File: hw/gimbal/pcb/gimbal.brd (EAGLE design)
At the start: 60 x 42 mm, 79 parts, among them J1 JST-XH4SMT_RA, U1 STM32F4R_64PIN, U2 TPS62172PWSON8, U3 TPS55330PQFN16, U4 MC33926, U5 DRV8313, U6 DRV8313, U7 AS5048A

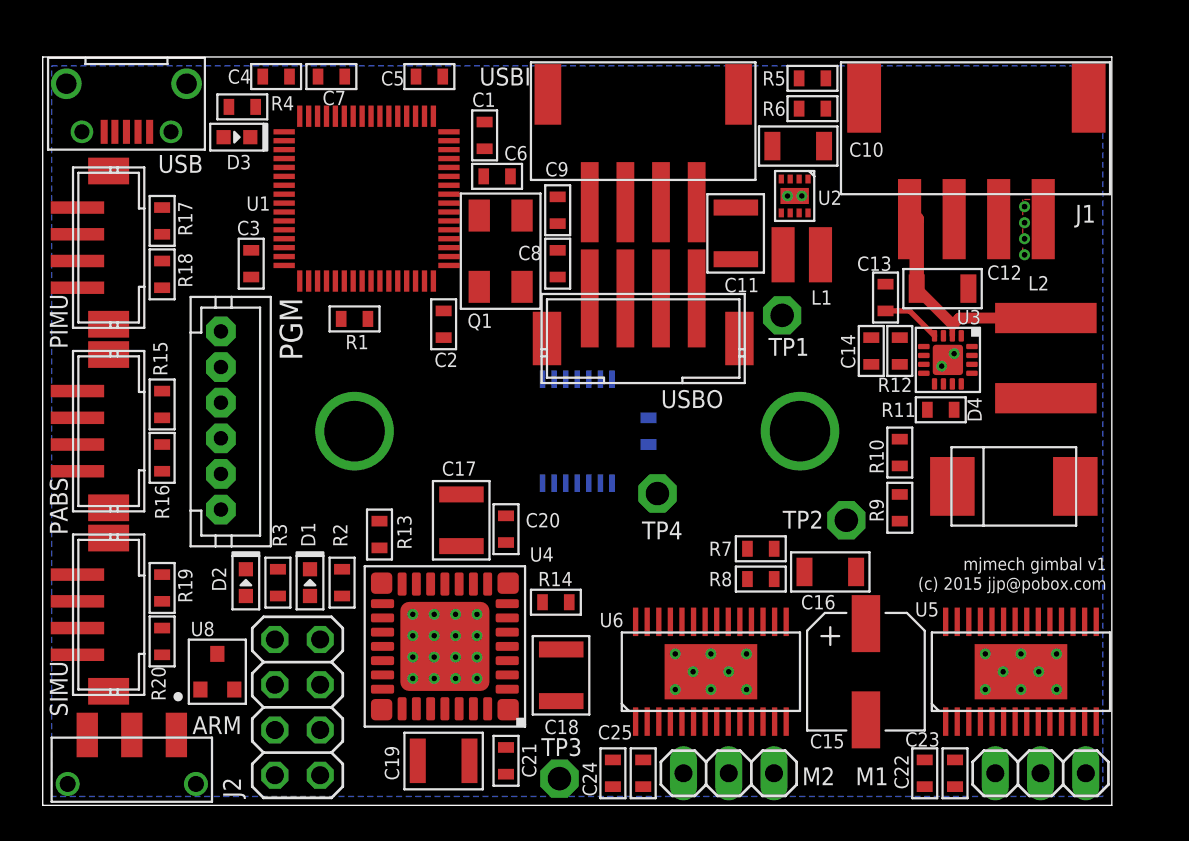
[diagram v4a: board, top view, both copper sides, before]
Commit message: gimbal board: Continued work on routing power.
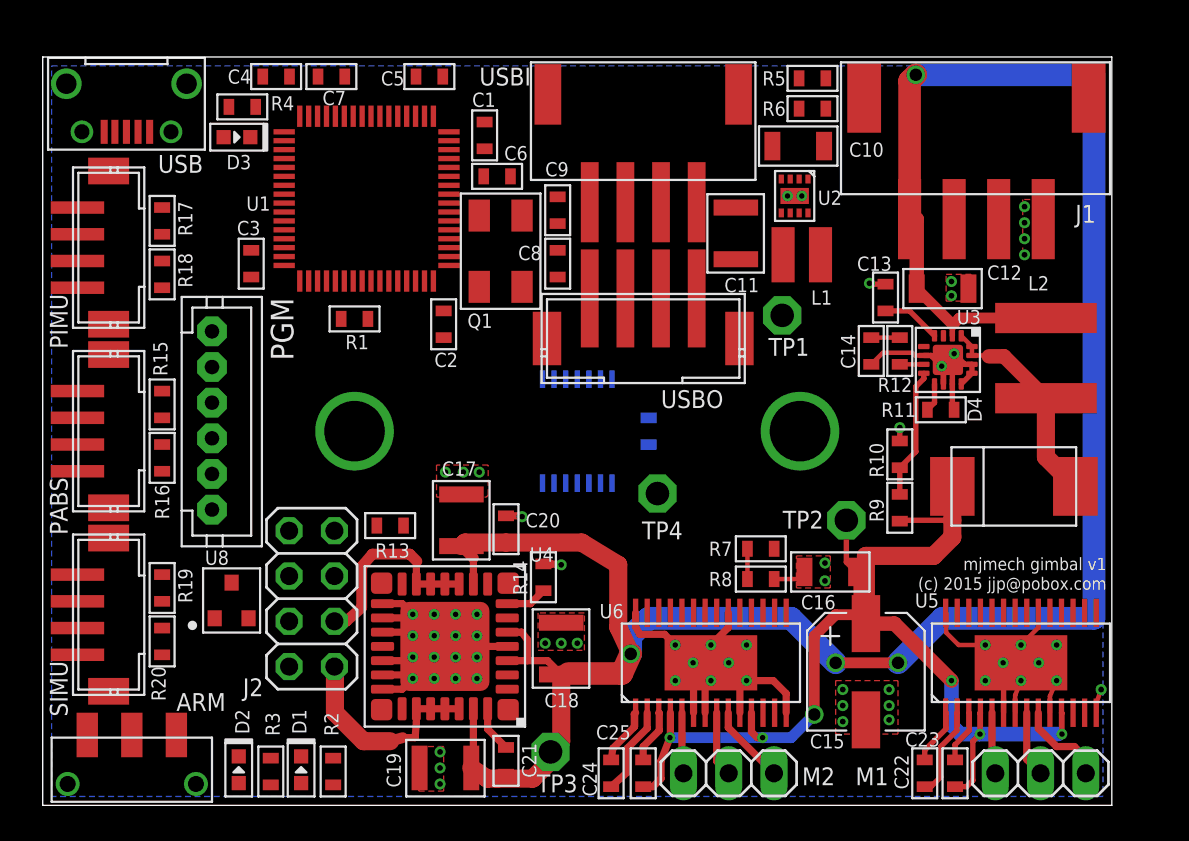
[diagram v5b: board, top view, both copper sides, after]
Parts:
- moved R2 10.6 mm to (16.3, 1.90)
- moved R3 10.6 mm to (12.8, 1.90)
- moved D1 10.5 mm to (14.5, 2.00)
- moved D2 10.5 mm to (11.0, 2.00)
- moved J2 6.15 mm to (15.1, 11.6)
- moved U8 4.08 mm to (10.6, 11.5)
- moved TP3 1.58 mm to (28.5, 3.00)
- moved R14 1.57 mm to (28.1, 12.8), turned to 270 degrees
- moved C18 1.50 mm to (29.1, 8.80)
- moved R13 0.78 mm to (19.5, 15.7), turned to 0 degrees
- moved PGM 0.50 mm to (9.50, 21.6)
- moved U5 0.50 mm to (54.9, 8.00)
- moved U6 0.50 mm to (37.5, 8.00)
- moved C19 0.41 mm to (22.6, 2.10)
- moved C25 0.10 mm to (31.9, 1.80)
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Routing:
- net +8V: track 13.2 -> 133.4 mm, vias 0 -> 4
- net +12V: track 0.00 -> 65.2 mm, vias 0 -> 6
- net GND: track 0.00 -> 61.6 mm, vias 4 -> 28
- net N$17: track 0.00 -> 12.1 mm
- net N$3: track 0.00 -> 11.8 mm
- net N$2: track 0.00 -> 11.4 mm
- net N$22: track 0.00 -> 7.36 mm
- net N$27: track 0.00 -> 5.11 mm
- net N$8: track 0.00 -> 5.09 mm
- net N$26: track 0.00 -> 5.02 mm
- net N$11: track 0.00 -> 4.46 mm
- net N$7: track 0.00 -> 3.72 mm
- net N$10: track 0.00 -> 3.68 mm
- net N$6: track 0.00 -> 3.48 mm
- net N$9: track 0.00 -> 3.44 mm
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
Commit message: gimbal board: More power routing.  Most ground pins have vias down to the ground plane now.
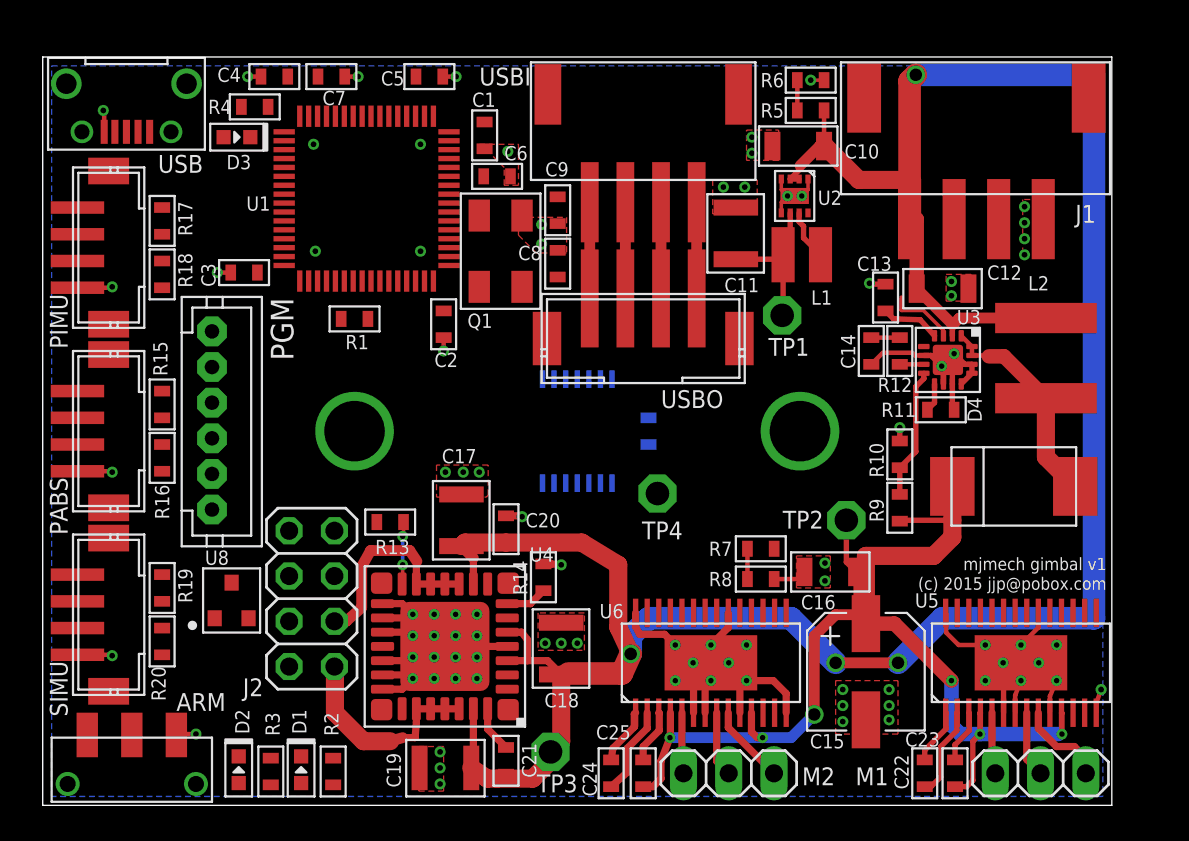
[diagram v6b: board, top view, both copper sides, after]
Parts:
- moved R5 1.80 mm to (43.1, 39.0)
- moved R6 1.60 mm to (43.1, 40.7)
- moved R4 0.70 mm to (11.9, 39.2)
- moved C3 0.64 mm to (11.3, 29.9), turned to 180 degrees
- moved R13 0.20 mm to (19.5, 15.9)
- moved C4 0.10 mm to (13.0, 40.9), turned to 180 degrees
- turned C10 to 180 degrees
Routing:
- net GND: track 61.6 -> 77.6 mm, vias 28 -> 50
- net +3V3: track 0.00 -> 12.2 mm, vias 0 -> 2
- net +8V: track 133.4 -> 144.4 mm
- net N$15: track 0.00 -> 5.40 mm
- net N$14: track 0.00 -> 5.40 mm
- net N$13: track 0.00 -> 5.40 mm
- net N$12: track 0.00 -> 5.40 mm
- net BOOST_EN: track 0.00 -> 3.83 mm
- net N$16: track 0.00 -> 2.85 mm
- net N$34: track 0.00 -> 1.70 mm

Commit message: gimbal board: Final draft of all routing and silks.
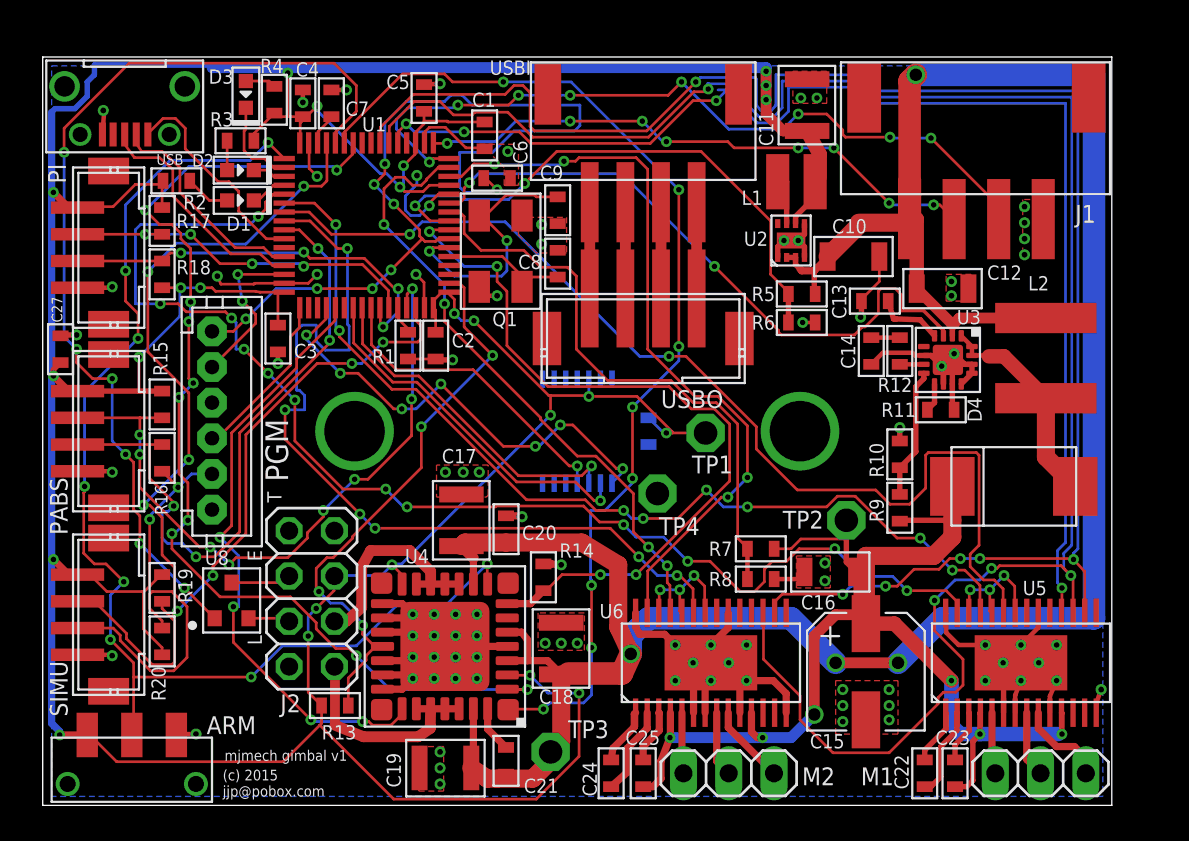
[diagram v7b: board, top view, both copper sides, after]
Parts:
- added C27: 0.1uF, mfpassives:C0603
- moved R3 35.4 mm to (11.1, 37.3), turned to 0 degrees
- moved R2 34.3 mm to (7.50, 35.0), turned to 180 degrees
- moved D2 33.7 mm to (11.1, 35.6), turned to 180 degrees
- moved D1 32.1 mm to (11.1, 34.0), turned to 180 degrees
- moved R6 13.6 mm to (42.6, 27.1)
- moved R13 10.8 mm to (16.4, 5.60), turned to 180 degrees
- moved R5 10.3 mm to (42.6, 28.7)
- moved C11 8.24 mm to (42.9, 39.3)
- moved TP1 7.88 mm to (37.2, 20.9)
- moved C10 6.93 mm to (45.5, 30.8), turned to 0 degrees
- moved C3 4.16 mm to (13.2, 26.2), turned to 270 degrees
- moved L1 4.11 mm to (42.3, 35.0), turned to 0 degrees
- moved R1 3.35 mm to (20.5, 25.8), turned to 90 degrees
- moved U2 2.51 mm to (42.0, 31.7), turned to 90 degrees
- moved D3 2.45 mm to (11.4, 39.9), turned to 90 degrees
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- renumbered PIMU to PI
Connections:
- net +3V3: now also C27.P$1
- net AS5048_CS: now also U1.52; no longer U1.20
- net AS5048_MISO: now also U1.56; no longer U1.22
- net AS5048_MOSI: now also U1.57; no longer U1.23
- net AS5048_SCK: now also U1.55; no longer U1.21
- net BLDC_FAULT1: now also U1.21; no longer U1.51
- net BLDC_FAULT2: no longer U1.40
- net BLDC_RESET/: now also U1.23; no longer U1.4
- net BLDC_SLEEP/: now also U1.22; no longer U1.3
- net BOOST_EN: now also U1.11; no longer U1.52
- net GND: now also C27.P$2
- net MOTOR2_IN3: now also U1.40; no longer U1.16
- net SLAVE_RX: now also U1.17; no longer U1.55
- net SLAVE_TX: now also U1.16; no longer U1.50
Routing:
- net +3V3: track 12.2 -> 262.6 mm, vias 2 -> 26
- net BLDC_SLEEP/: track 0.00 -> 108.4 mm, vias 0 -> 4
- net BLDC_RESET/: track 0.00 -> 96.9 mm, vias 0 -> 6
- net BLDC_FAULT1: track 0.00 -> 73.3 mm, vias 0 -> 4
- net MOTOR1_IN1: track 0.00 -> 71.9 mm, vias 0 -> 12
- net MOTOR_EN: track 0.00 -> 67.8 mm, vias 0 -> 8
- net AEG_PWM: track 0.00 -> 60.0 mm, vias 0 -> 10
- net MOTOR1_IN3: track 0.00 -> 59.7 mm, vias 0 -> 2
- net AGITATOR_PWM: track 0.00 -> 59.3 mm, vias 0 -> 8
- net MOTOR1_IN2: track 0.00 -> 55.0 mm, vias 0 -> 8
- net LASER_EN: track 0.00 -> 53.8 mm, vias 0 -> 6
- net SIMU_SCL: track 0.00 -> 50.5 mm, vias 0 -> 4
- net MOTOR2_IN3: track 0.00 -> 49.3 mm, vias 0 -> 6
- net N$24: track 0.00 -> 49.0 mm, vias 0 -> 8
- net SLAVE_TX: track 0.00 -> 43.5 mm, vias 0 -> 8
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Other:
- board text added: "E"
- board text added: "L"
- board text added: "T"

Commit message: gimbal: pcb: Fix the STM32 footprint.  * ripup all autorouted things, (and actually trace with that size)  * change all manually routed vias to have a slightly unique size  * move stuff around so at least it doesn't overlap, although it is    really ready to route again
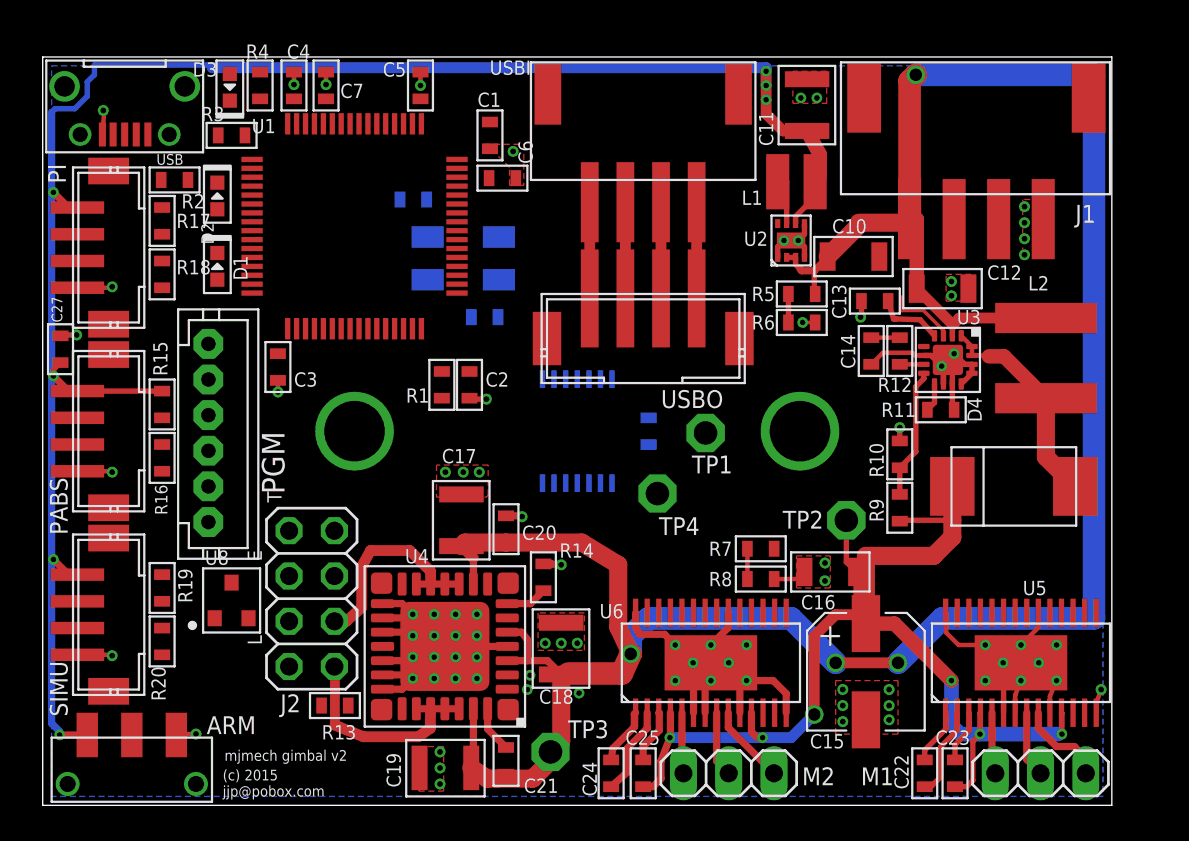
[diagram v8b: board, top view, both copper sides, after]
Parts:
- moved C9 8.12 mm to (20.8, 34.0), flipped to the bottom, turned to 0 degrees
- moved C8 5.08 mm to (24.8, 27.4), flipped to the bottom, turned to 0 degrees
- moved D1 3.92 mm to (9.80, 30.2), turned to 270 degrees
- moved C2 2.91 mm to (23.9, 23.6)
- moved R1 2.91 mm to (22.4, 23.6)
- moved Q1 2.14 mm to (23.6, 30.7), flipped to the bottom, turned to 0 degrees
- moved D2 1.95 mm to (9.80, 34.2), turned to 270 degrees
- moved C3 1.60 mm to (13.2, 24.6)
- moved R4 1.13 mm to (12.2, 40.4)
- moved C4 1.12 mm to (14.1, 40.4)
- moved C7 1.04 mm to (15.9, 40.4)
- moved U1 1.00 mm to (17.5, 32.5), turned to 180 degrees
- moved D3 0.98 mm to (10.5, 40.3)
- moved PGM 0.73 mm to (9.30, 20.9)
- moved C5 0.73 mm to (21.2, 40.4)
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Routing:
- net +3V3: track 262.6 -> 101.7 mm, vias 26 -> 9
- net BLDC_SLEEP/: track 108.4 -> 0.00 mm, vias 4 -> 0
- net BLDC_RESET/: track 96.9 -> 0.00 mm, vias 6 -> 0
- net BLDC_FAULT1: track 73.3 -> 0.00 mm, vias 4 -> 0
- net MOTOR1_IN1: track 71.9 -> 0.00 mm, vias 12 -> 0
- net MOTOR_EN: track 67.8 -> 0.00 mm, vias 8 -> 0
- net AEG_PWM: track 60.0 -> 0.00 mm, vias 10 -> 1
- net MOTOR1_IN3: track 59.7 -> 0.00 mm, vias 2 -> 0
- net AGITATOR_PWM: track 59.3 -> 0.00 mm, vias 8 -> 0
- net MOTOR1_IN2: track 55.0 -> 0.00 mm, vias 8 -> 0
- net LASER_EN: track 53.8 -> 0.00 mm, vias 6 -> 0
- net SIMU_SCL: track 50.5 -> 0.00 mm, vias 4 -> 0
- net MOTOR2_IN3: track 49.3 -> 0.00 mm, vias 6 -> 0
- net N$24: track 49.0 -> 0.00 mm, vias 8 -> 0
- net SLAVE_TX: track 43.5 -> 0.00 mm, vias 8 -> 0
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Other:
- board text added: "mjmech gimbal v2"
- board text removed: "mjmech gimbal v1"
